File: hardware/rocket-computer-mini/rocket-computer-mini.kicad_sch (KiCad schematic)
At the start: 18 parts, among them U1 FSUSB63UMX

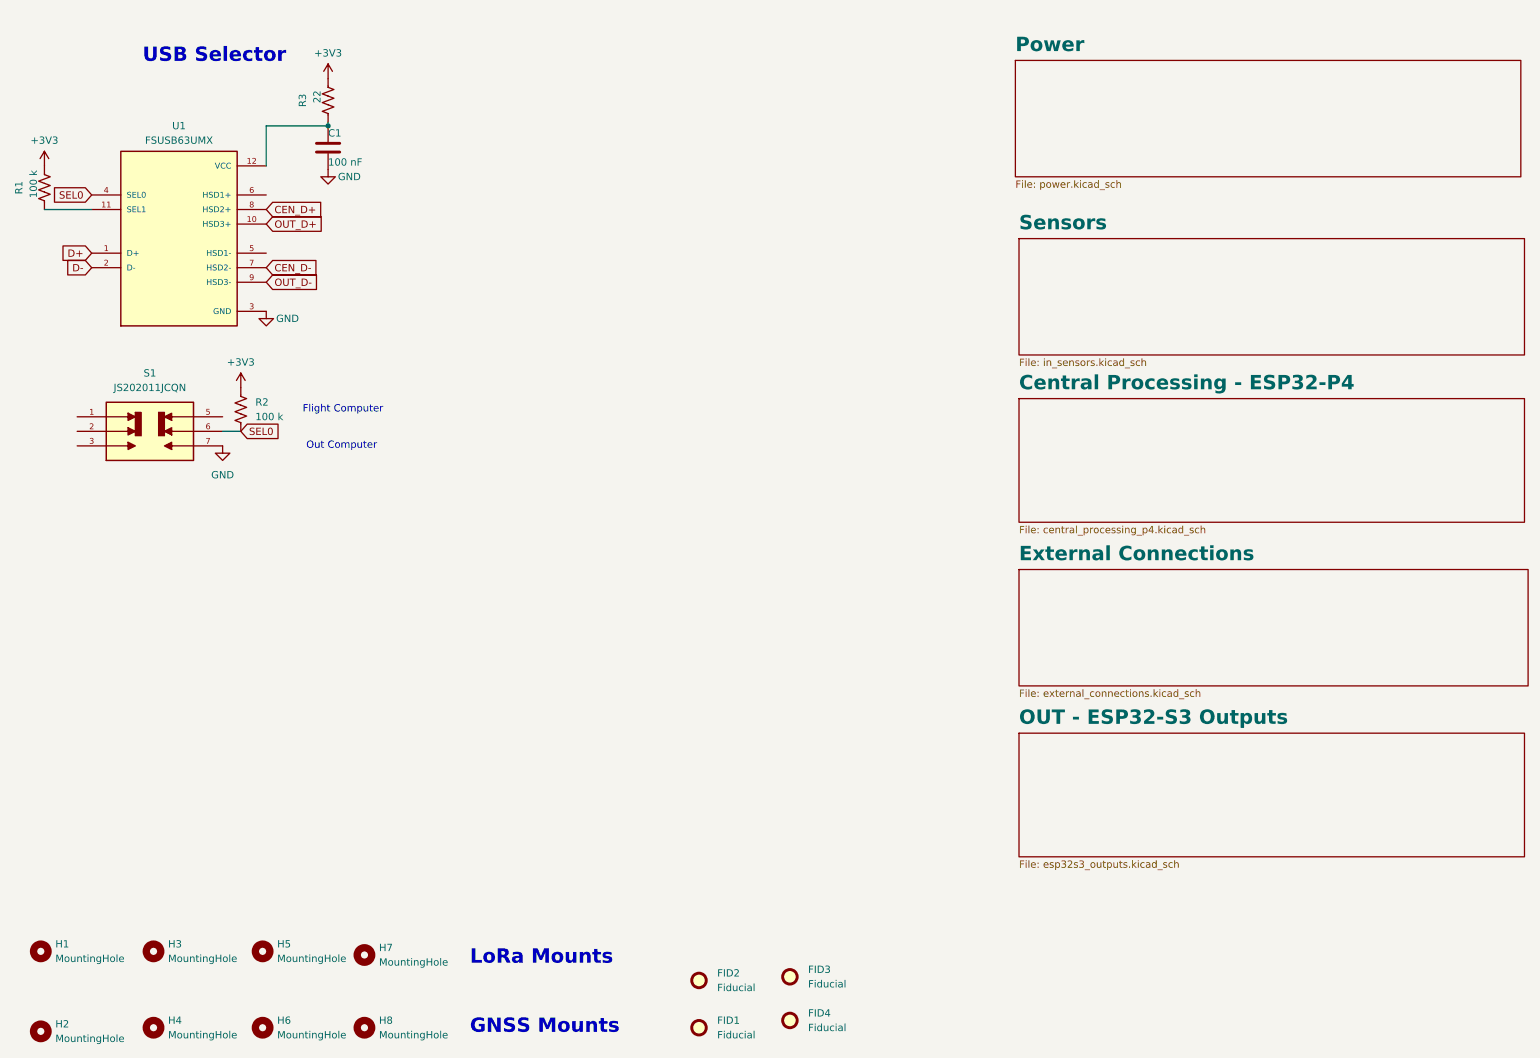
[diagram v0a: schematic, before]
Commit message: hardware: rocket-computer-mini drops the ESP32-P4, S3 becomes MCU
First reduction pass. The ESP32-P4 is removed entirely and the ESP32-S3 is now
the only processor on the board, so it is no longer called OUT.

Removed -- the whole Central Processing - ESP32-P4 sheet, 65 parts: U17 (the
P4), U16 its SPI flash, U20 its dedicated TLV62569 buck, Y3/Y4 its crystals,
SW2, LEDs D7/D8 and 57 passives. Parts 255 -> 190, nets 234 -> 191, sheets
5 -> 4. Schematic and PCB both land on 190; no reference to the P4 sheet
remains in either.

Renamed -- sheet OUT - ESP32-S3 Outputs becomes MCU - ESP32-S3 in
esp32s3_mcu.kicad_sch, and the nine OUT_* nets become MCU_*. Pin names that
merely contain OUT (VOUT, OUT_17, Net-(U28-OUT)) were matched on the full
quoted net name so they were left untouched. The power-sheet note claiming
"ESP32-OUT ... enables Flight Computer" described the S3 gating the P4 and was
reworded; the topology behind it has not been rethought.

PCB -- the 65 footprints deleted, then 419 copper items (400 segments, 19
vias) removed from the 43 nets left with no pads at all, then zones refilled.

Known and deliberate: the P4 owned nearly every subsystem, so 34 named signals
are now down to a single endpoint -- sensors, all four pyro channels, all
twelve EXP lines, camera, piezo, servo, the ESP_* link and P4_EN_HOLD. Nothing
is rewired to the S3 yet and the board cannot fly as it stands.

DRC goes 28 -> 88 and every pre-existing category went down; the whole rise is
66 track_dangling + 2 via_dangling, stubs to former P4 pads on nets that still
have pads elsewhere. Left in place: these nets are about to be rewired and the
region re-laid-out, so trimming now is work the next pass would discard.
Unconnected is still 0, ERC 1012 -> 823, parity 11 -> 8.

Also stale, recorded not fixed: bom.csv is still V9's 255-part BOM, and the
on-board fab note still cites QFN-104 (U17) as the reason for ENIG.

Co-Authored-By: Claude Opus 5 <noreply@anthropic.com>
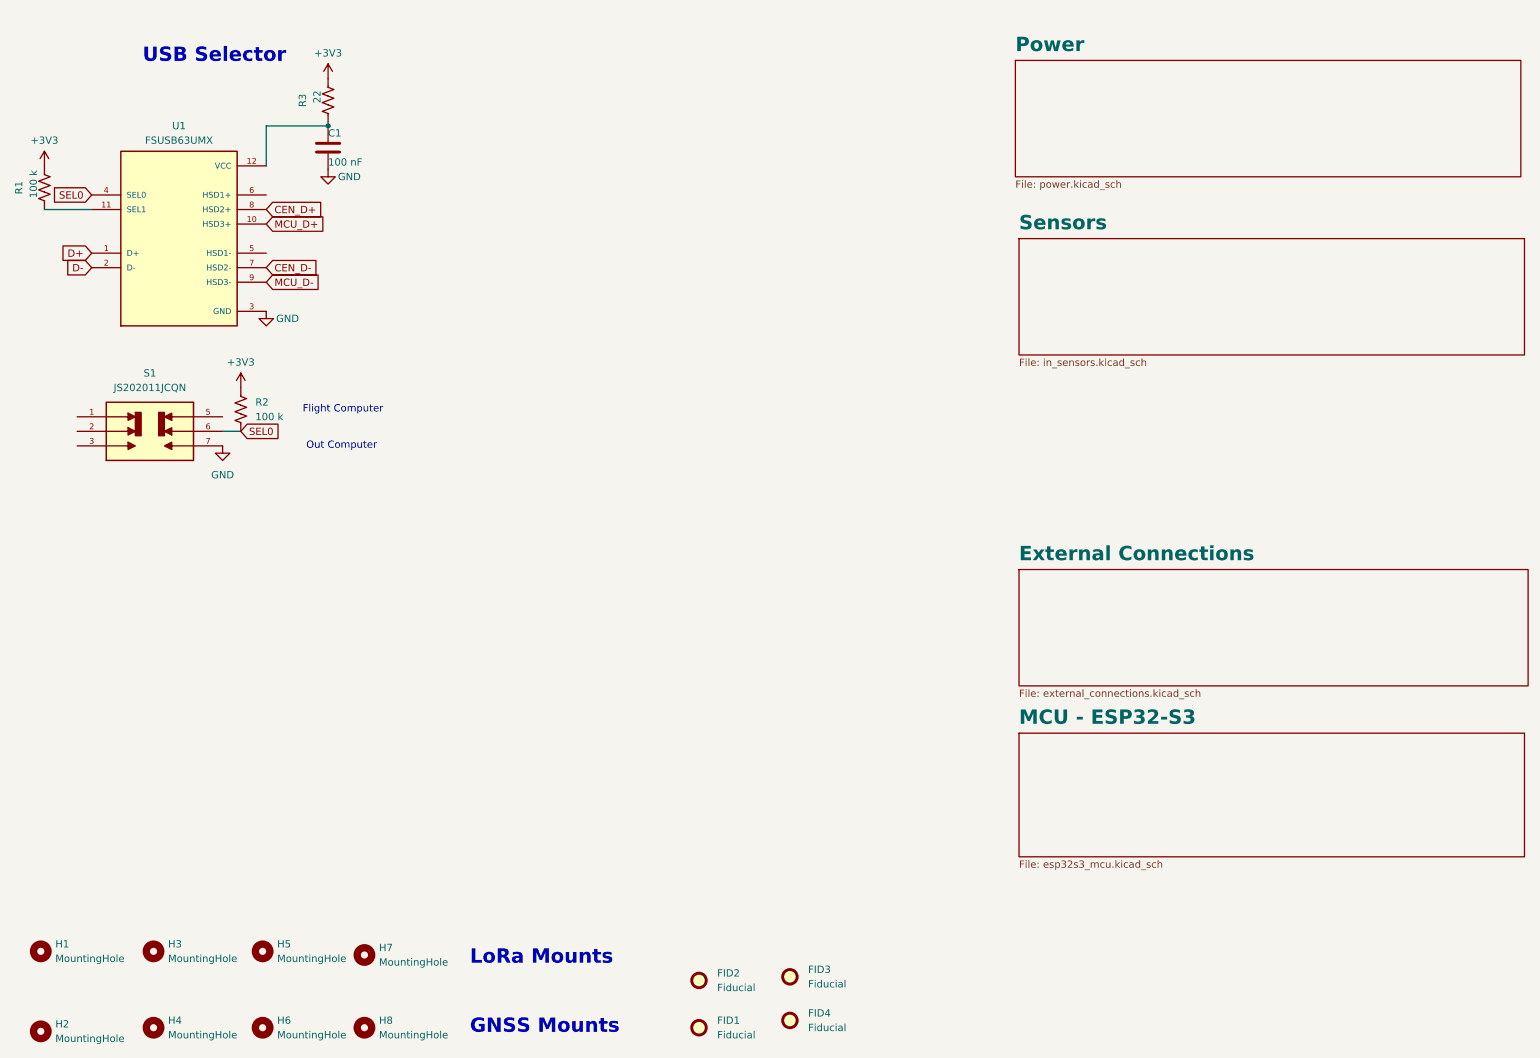
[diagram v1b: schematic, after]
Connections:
- net OUT_D+ renamed MCU_D+
- net OUT_D- renamed MCU_D-
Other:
- sheet OUT - ESP32-S3 Outputs renamed MCU - ESP32-S3
- removed sheet Central Processing - ESP32-P4
- sheet MCU - ESP32-S3: file esp32s3_outputs.kicad_sch -> esp32s3_mcu.kicad_sch
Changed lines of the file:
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@@
 		)
 	)
-	(global_label "OUT_D-"
+	(global_label "MCU_D-"
 		(shape input)
 		(at 57.15 62.865 0)
@@
 		)
 	)
-	(global_label "OUT_D+"
+	(global_label "MCU_D+"
 		(shape input)
 		(at 57.15 52.705 0)
@@
 	)
 	(sheet
-		(at 188.595 83.185)
+		(at 188.595 141.605)
 		(size 88.265 21.59)
 		(exclude_from_sim no)
@@
 			(color 0 0 0 0)
 		)
-		(property "Sheetname" "Central Processing - ESP32-P4"
-			(at 188.595 81.8584 0)
-			(show_name no)
-			(do_not_autoplace no)
-			(effects
-				(font
-					(size 2.5 2.5)
-					(thickness 0.5)
-					(bold yes)
-				)
-				(justify left bottom)
-			)
-		)
-		(property "Sheetfile" "central_processing_p4.kicad_sch"
-			(at 188.595 105.3596 0)
-			(show_name no)
-			(do_not_autoplace no)
-			(effects
-				(font
-					(size 1.27 1.27)
-				)
-				(justify left top)
-			)
-		)
-		(instances
-			(project "rocket-computer-mini"
-				(path "/ae61c2c4-72e9-4776-93ae-2e716b9dc70f"
-					(page "6")
-				)
-			)
-		)
-	)
-	(sheet
-		(at 188.595 141.605)
-		(size 88.265 21.59)
-		(exclude_from_sim no)
-		(in_bom yes)
-		(on_board yes)
-		(dnp no)
-		(fields_autoplaced yes)
-		(stroke
-			(width 0.1524)
-			(type solid)
-		)
-		(fill
-			(color 0 0 0 0)
-		)
-		(property "Sheetname" "OUT - ESP32-S3 Outputs"
+		(property "Sheetname" "MCU - ESP32-S3"
 			(at 188.595 140.2784 0)
 			(show_name no)
@@
 			)
 		)
-		(property "Sheetfile" "esp32s3_outputs.kicad_sch"
+		(property "Sheetfile" "esp32s3_mcu.kicad_sch"
 			(at 188.595 163.7796 0)
 			(show_name no)

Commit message: hardware: rocket-computer-mini gains the on-board radio, sheds more parts
Second reduction pass, plus the radio moves on-board.

Added: the 900 MHz radio module (U16) and its two decoupling caps, wired for
direct SPI rather than through the daughterboard connector. Removed: 31
designators including the camera connector (J4), the piezo (LS1), mounting
hardware (H5-H8), and the support parts that went with them. Also gone are the
magnetometer interrupt and the inertial sensor's second interrupt -- neither was
ever used by firmware, which is what made them free to drop.

Parts 190 -> 161, nets 191 -> 165.

Adds a pin budget for the reduced board (pin-budget.md). The headline is that
the board fits, but not comfortably: 23 signals against 27 usable pads, and only
16 of those pads are free of strapping, console, JTAG or flash-adjacent duty.

Three findings shaped it:

- The radio needs seven pins, not nine. DIO2 drives transmit-enable inside the
  module and needs no processor pin; receive-enable is floating and has no
  firmware pin at all. The out-computer firmware still carries the direct-SPI
  driver from the V7 topology and defines exactly those seven, so putting the
  bare module back on-board is a board change rather than a firmware rewrite.
- Pyro continuity is a digital read, not analogue, and nothing on this board
  needs an ADC channel -- so the ADC2-versus-radio restriction does not
  constrain the design.
- Continuity belongs on an I2C expander, not a multiplexer. A four-to-one mux
  needs two select lines plus data, saving one pin; the expander shares the bus
  the magnetometer is joining and saves four.

The proposed assignment keeps the serial console free and spends JTAG. Pyro
firing is confined to unrestricted pins -- never a strapping pin and never one
the boot ROM drives, since the console transmit pin is active on every boot.

One assumption can invalidate it: three signals sit on flash-adjacent pads that
are free only if the package carries no in-pa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
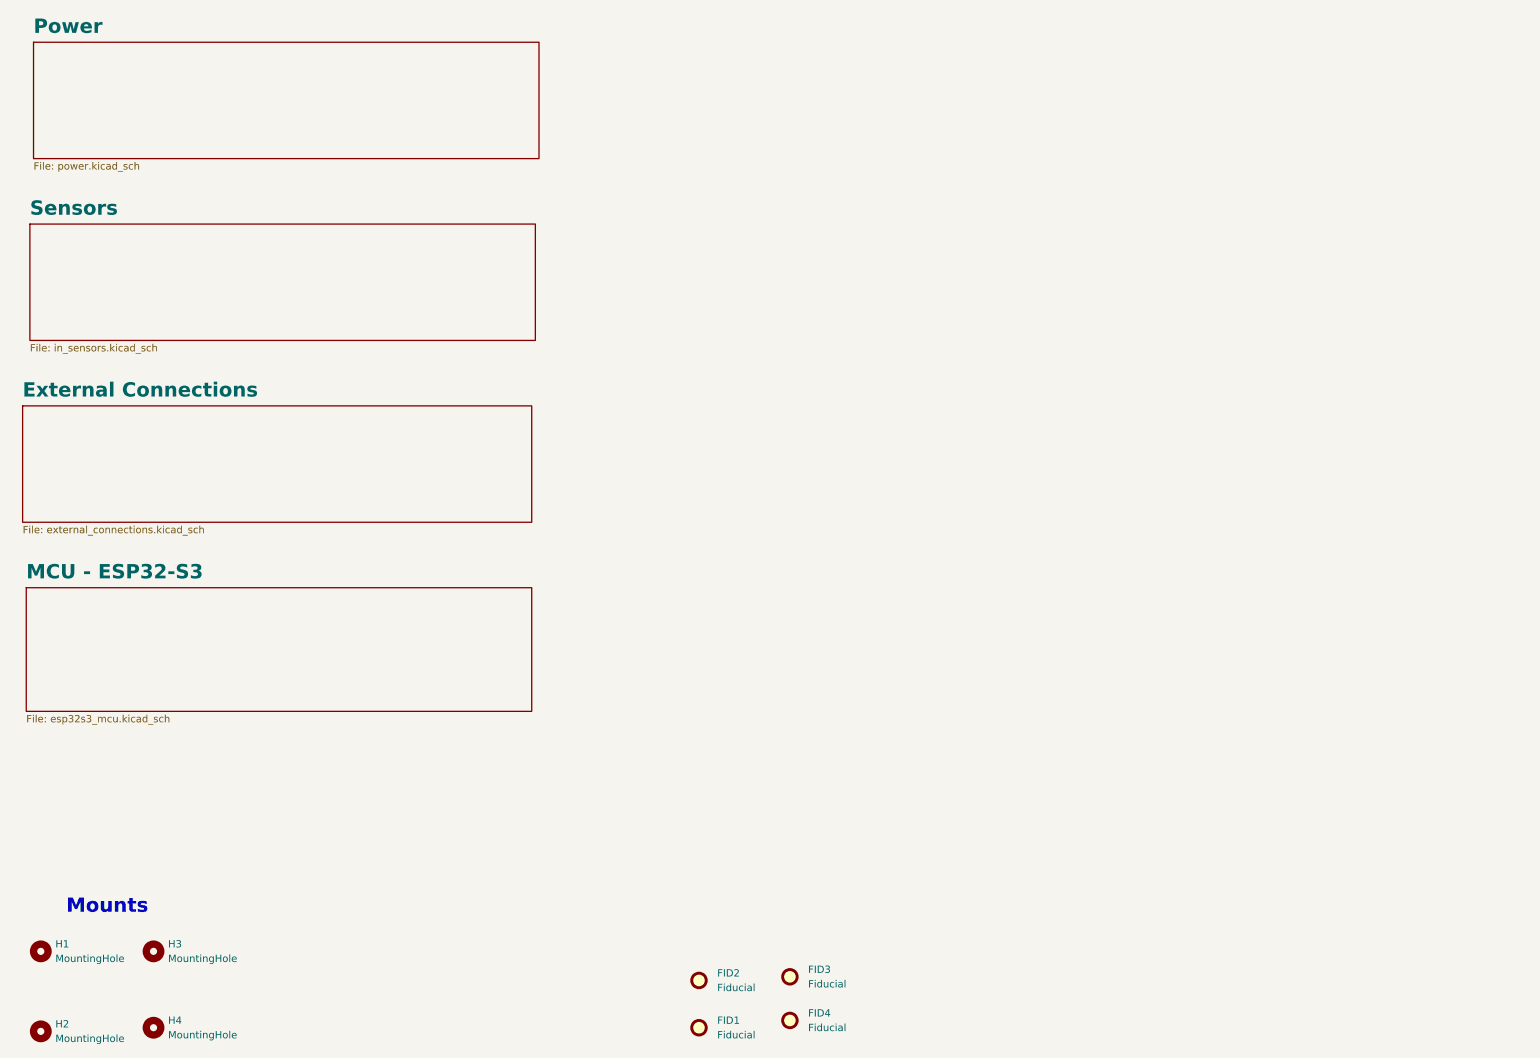
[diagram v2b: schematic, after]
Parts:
- removed C1: 100 nF, Capacitor_SMD:C_0402_1005Metric, symbol Device:C
- removed H5, H6, H7, H8: MountingHole, MountingHole:MountingHole_2.2mm_M2_DIN965_Pad_TopBottom, symbol Mechanical:MountingHole
- removed R1, R2: 100 k, Resistor_SMD:R_0402_1005Metric, symbol Device:R_US
- removed R3: 22, Resistor_SMD:R_0402_1005Metric, symbol Device:R_US
- removed S1: JS202011JCQN, Footprints:SW_JS202011JCQN, symbol Custom:JS202011JCQN
- removed U1: FSUSB63UMX, Footprints:QFN40P180X180X55-12N, symbol Custom:FSUSB63UMX
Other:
- note added: "Mounts"
- note removed: "Flight Computer"
- note removed: "GNSS Mounts"
- note removed: "LoRa Mounts"
- note removed: "Out Computer"
- note removed: "USB Selector"

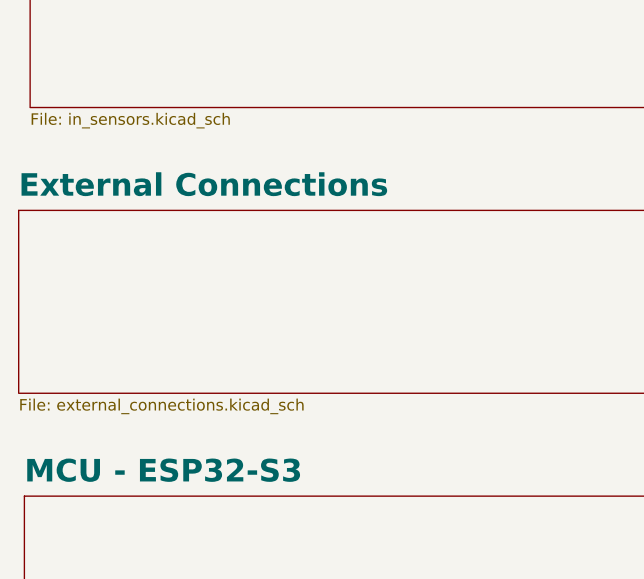
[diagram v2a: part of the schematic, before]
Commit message: hardware: rename the External Connections sheet to Pyro, wire up the 3D models
Two changes that both needed the KiCad session closed.

The External Connections sheet becomes Pyro, in pyro.kicad_sch. The old name
described a sheet that carried the expansion header, camera, servo and piezo
alongside the pyro channels; all of those were removed during the reduction, so
the sheet now carries the four pyro channels and little else. Renamed in the root
schematic, in the project file's sheet list, and across 78 footprint sheetname
and sheetfile properties in the PCB, with the file moved to match.

The two 3D models added earlier are now referenced from their footprints, at
zero offset and rotation -- both were drawn at the footprint origin so they need
no transform. Paths resolve through ${KIPRJMOD}/../3dmodels/ like the other 63.

Verified: the netlist exports cleanly at 157 parts and the sheet path now reads
/Pyro/ alongside /Sensors/, /Power/ and /MCU - ESP32-S3/. No reference to the old
name survives anywhere in the board directory.

Note on the DRC numbers, which look alarming and are not from this change: the
board file currently holds zero net declarations and zero track segments, so DRC
reports every connection as missing. The layout has not been resynced since the
processor removal. That is known and separate.

Also corrects the README, which still described the sheet set as it stood at the
fork.

Co-Authored-By: Claude Opus 5 <noreply@anthropic.com>
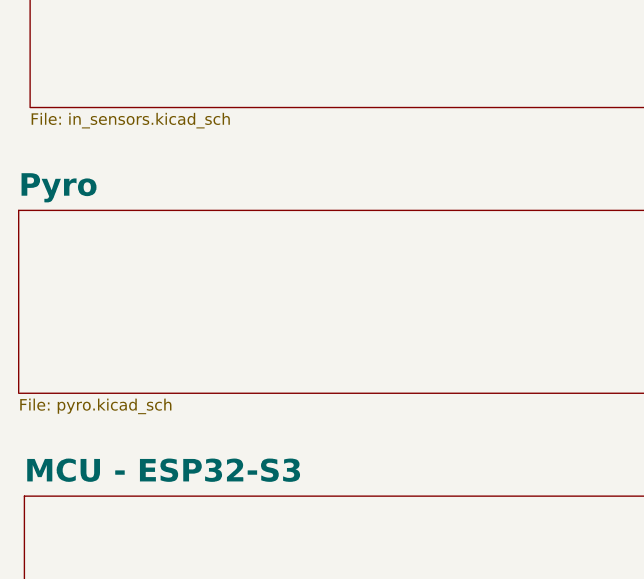
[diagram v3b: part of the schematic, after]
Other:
- sheet External Connections renamed Pyro
- sheet Pyro: file external_connections.kicad_sch -> pyro.kicad_sch
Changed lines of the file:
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@@
 			(color 0 0 0 0)
 		)
-		(property "Sheetname" "External Connections"
+		(property "Sheetname" "Pyro"
 			(at 14.605 83.1284 0)
 			(show_name no)
@@
 			)
 		)
-		(property "Sheetfile" "external_connections.kicad_sch"
+		(property "Sheetfile" "pyro.kicad_sch"
 			(at 14.605 105.3596 0)
 			(show_name no)
